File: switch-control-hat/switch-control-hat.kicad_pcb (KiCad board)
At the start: 2 copper layers, 85 x 56 mm, 45 parts, among them J1 Power Connector, J2 Frontend Connector, P1 RPi-Header, U1 MCP23017_SO, U10 TLP3543, U11 TLP3543, U12 TLP3543, U2 DS3231M, U3 TLP3543, U4 TLP3543, U5 TLP3543, U6 TLP3543, U7 TLP3543, U8 TLP3543, U9 TLP3543

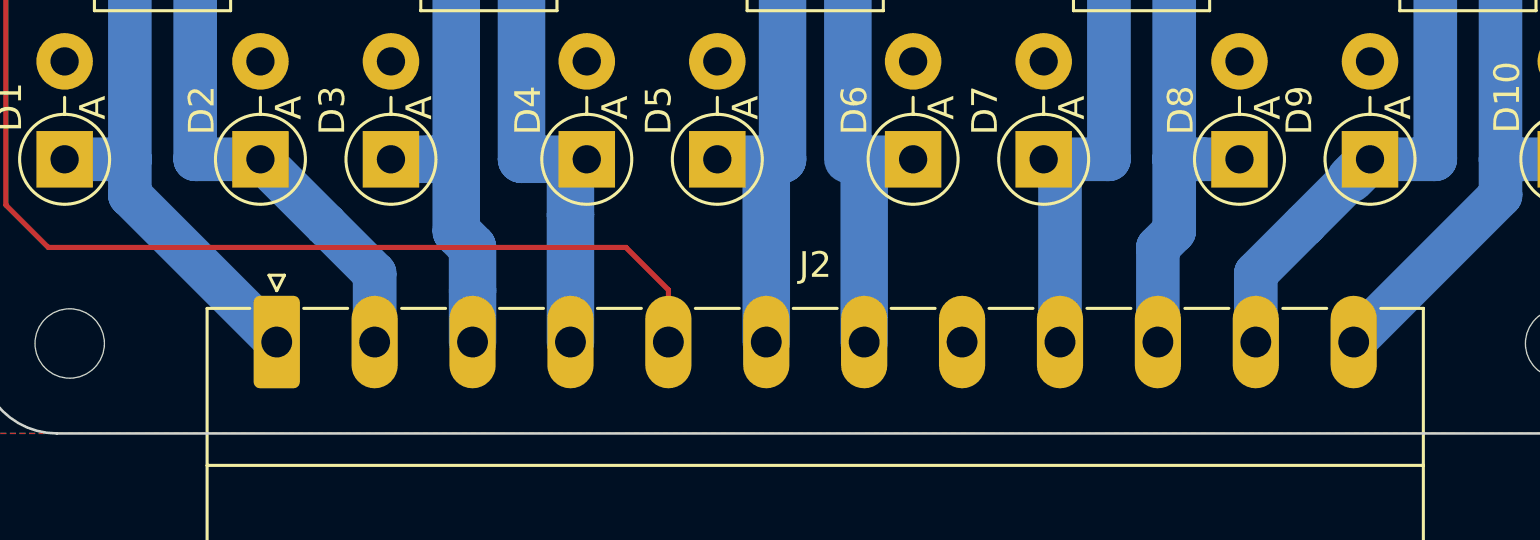
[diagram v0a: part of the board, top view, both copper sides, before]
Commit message: Added connector pin labels
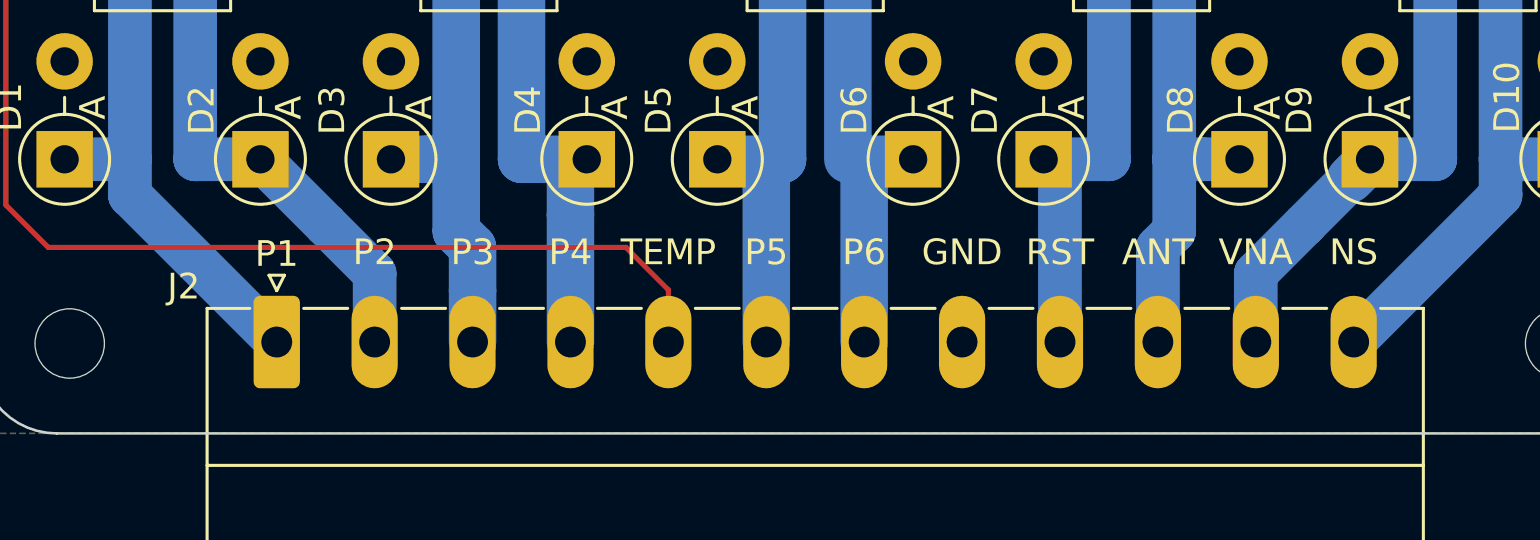
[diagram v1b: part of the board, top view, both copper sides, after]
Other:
- board text added: "ANT"
- board text added: "GND"
- board text added: "NS"
- board text added: "P1"
- board text added: "P2"
- board text added: "P3"
- board text added: "P4"
- board text added: "P5"
- board text added: "P6"
- board text added: "RST"
- board text added: "TEMP"
- board text added: "VNA"
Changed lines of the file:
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@@
   (general
     (thickness 1.6)
-    (drawings 10)
+    (drawings 22)
     (tracks 292)
     (zones 0)
@@
     (visible_elements 7FFFFFFF)
     (pcbplotparams
-      (layerselection 0x010b0_ffffffff)
+      (layerselection 0x010f0_ffffffff)
       (usegerberextensions true)
       (usegerberattributes false)
@@
     (descr "Generic Phoenix Contact connector footprint for: MC_1,5/12-G-3.81; number of pins: 12; pin pitch: 3.81mm; Angled || order number: 1803374 8A 160V")
     (tags "phoenix_contact connector MC_01x12_G_3.81mm")
-    (fp_text reference J2 (at 20.96 -3) (layer F.SilkS)
+    (fp_text reference J2 (at -3.6195 -2.159) (layer F.SilkS)
       (effects (font (size 1 1) (thickness 0.15)))
     )
@@
     (pad 1 np_thru_hole circle (at 0 0 180) (size 2.7 2.7) (drill 2.7) (layers *.Cu *.Mask))
   )
+  (gr_text NS (at 253.467 142.9515) (layer F.SilkS)
+    (effects (font (size 1 1) (thickness 0.15)))
+  )
+  (gr_text VNA (at 249.657 142.9515) (layer F.SilkS)
+    (effects (font (size 1 1) (thickness 0.15)))
+  )
+  (gr_text ANT (at 245.847 142.9515) (layer F.SilkS)
+    (effects (font (size 1 1) (thickness 0.15)))
+  )
+  (gr_text RST (at 242.037 142.9515) (layer F.SilkS)
+    (effects (font (size 1 1) (thickness 0.15)))
+  )
+  (gr_text GND (at 238.227 142.9515) (layer F.SilkS)
+    (effects (font (size 1 1) (thickness 0.15)))
+  )
+  (gr_text P6 (at 234.417 142.9515) (layer F.SilkS)
+    (effects (font (size 1 1) (thickness 0.15)))
+  )
+  (gr_text P5 (at 230.607 142.9515) (layer F.SilkS)
+    (effects (font (size 1 1) (thickness 0.15)))
+  )
+  (gr_text P1 (at 211.557 143.015) (layer F.SilkS)
+    (effects (font (size 1 1) (thickness 0.15)))
+  )
+  (gr_text P2 (at 215.367 142.9515) (layer F.SilkS)
+    (effects (font (size 1 1) (thickness 0.15)))
+  )
+  (gr_text P3 (at 219.177 142.9515) (layer F.SilkS)
+    (effects (font (size 1 1) (thickness 0.15)))
+  )
+  (gr_text P4 (at 222.987 142.9515) (layer F.SilkS)
+    (effects (font (size 1 1) (thickness 0.15)))
+  )
+  (gr_text TEMP (at 226.797 142.9515) (layer F.SilkS)
+    (effects (font (size 1 1) (thickness 0.15)))
+  )
   (gr_text "Nivek Ghazi" (at 278.74 137.3 90) (layer F.SilkS)
